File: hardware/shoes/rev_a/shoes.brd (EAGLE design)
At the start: 25.1 x 21.3 mm, 36 parts, among them J4 TC2030-JLINK-NL, Q1 MOSFET-NCHANNELXFDN-3, Q2 MOSFET-NCHANNELXFDN-3, Q3 MOSFET-NCHANNELXFDN-3, Q4 MOSFET-NCHANNELXFDN-3, U1 NRF51822QF, U2 ADXL362, X1 16MHz

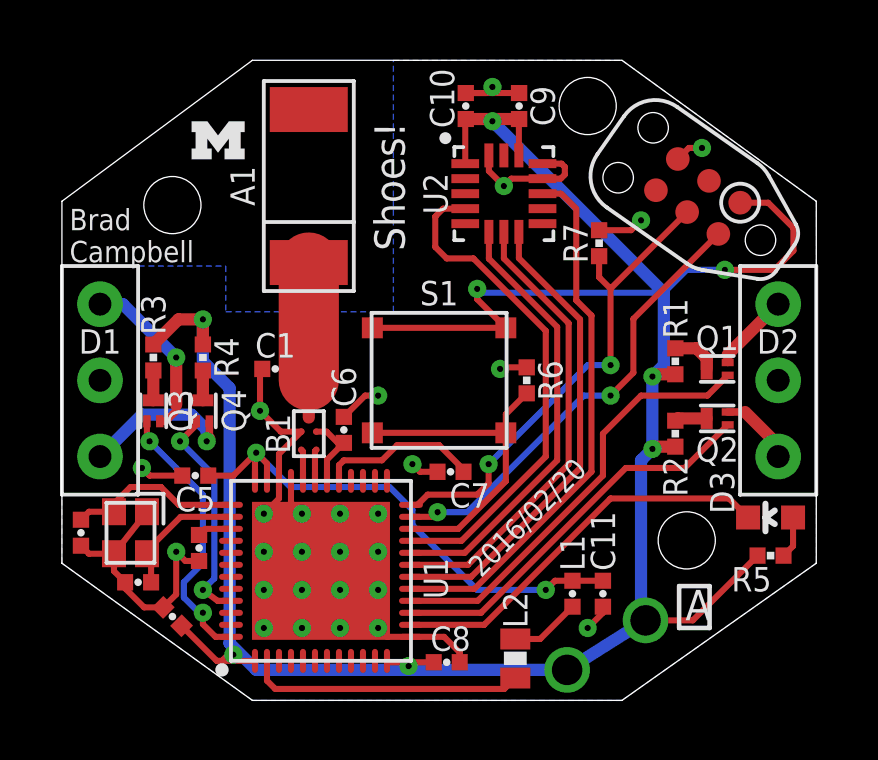
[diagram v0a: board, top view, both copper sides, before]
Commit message: board changes
added cap from power to ground
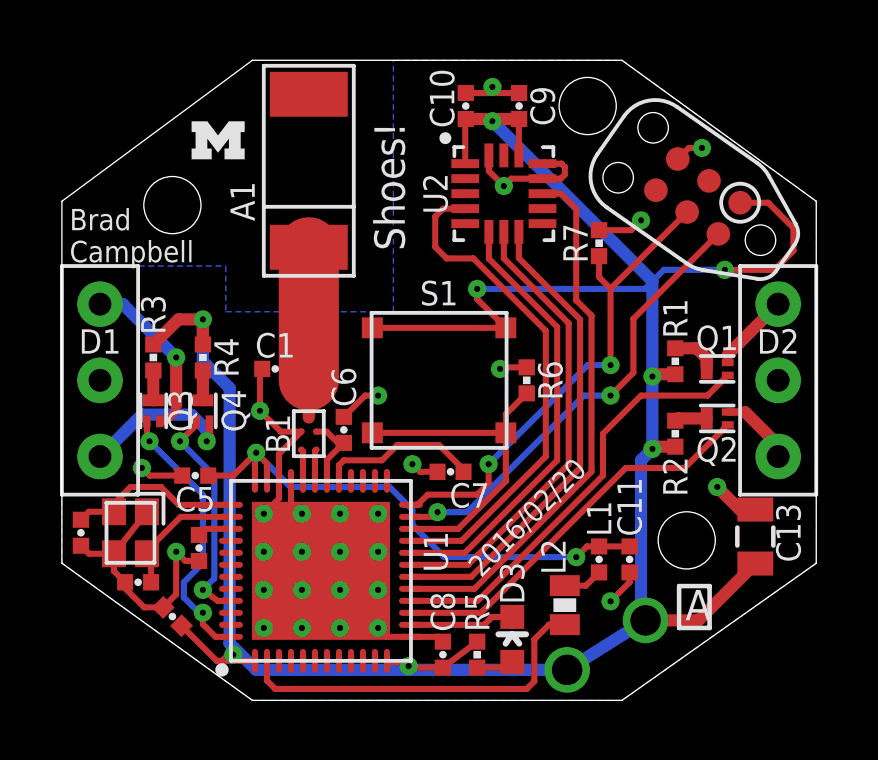
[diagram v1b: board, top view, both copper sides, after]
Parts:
- added C13: (no value), SparkFun-Capacitors:0805
- moved R5 10.3 mm to (1.27, -9.14), turned to 270 degrees
- moved D3 9.52 mm to (2.44, -8.64), turned to 0 degrees
- moved L2 2.43 mm to (4.19, -7.49)
- moved C11 1.45 mm to (6.35, -5.97)
- moved L1 1.45 mm to (5.33, -5.97)
- moved A1 0.51 mm to (-4.34, 6.99)
- moved C8 0.28 mm to (0.13, -9.14), turned to 90 degrees
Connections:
- net GND: now also C13.2
- net VCC: now also C13.1
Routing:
- net N$7: track 13.2 -> 3.48 mm
- net DCC: track 9.20 -> 12.4 mm
- net VCC: track 85.0 -> 86.0 mm
- net N$14: track 2.35 -> 1.33 mm
- net GND: track 36.0 -> 36.9 mm, vias 27 -> 28
- net N$11: track 6.14 -> 6.64 mm

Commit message: move antenna back
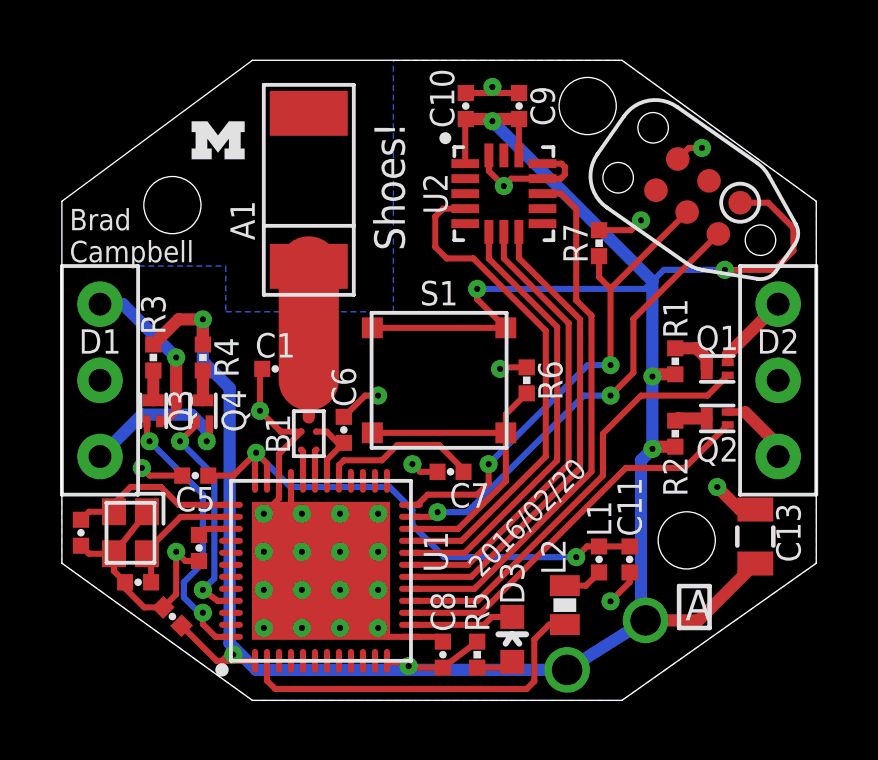
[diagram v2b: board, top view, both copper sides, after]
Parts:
- moved A1 0.64 mm to (-4.34, 6.35)
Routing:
- net N$11: track 6.64 -> 6.01 mm
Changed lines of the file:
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@@
 <attribute name="VALUE" x="-0.127" y="-9.144" size="1.016" layer="27" font="vector" ratio="12" rot="R270" align="bottom-center"/>
 </element>
-<element name="A1" library="chips" package="FRACTUS-ANTENNA-FR05-S1-N-0-102" value="FRACTUS-2.4GHZ-FR05-S1-N-0-102" x="-4.3434" y="6.985" smashed="yes" rot="R90">
-<attribute name="RICHARDSON_RFPD" value="FR05-S1-N-0102B" x="46.7106" y="-14.605" size="1.778" layer="27" rot="R90" display="off"/>
-<attribute name="NAME" x="-6.1434" y="5.969" size="0.8128" layer="25" font="vector" ratio="12" rot="R90" align="bottom-center"/>
+<element name="A1" library="chips" package="FRACTUS-ANTENNA-FR05-S1-N-0-102" value="FRACTUS-2.4GHZ-FR05-S1-N-0-102" x="-4.3434" y="6.35" smashed="yes" rot="R90">
+<attribute name="RICHARDSON_RFPD" value="FR05-S1-N-0102B" x="46.7106" y="-15.24" size="1.778" layer="27" rot="R90" display="off"/>
+<attribute name="NAME" x="-6.1434" y="5.334" size="0.8128" layer="25" font="vector" ratio="12" rot="R90" align="bottom-center"/>
 </element>
 <element name="L2" library="passives" package="0603_CAP" value="10uH" x="4.191" y="-7.493" smashed="yes" rot="R270">
@@
 <contactref element="A1" pad="1"/>
 <contactref element="C1" pad="1"/>
-<wire x1="-4.3434" y1="4.435" x2="-4.3434" y2="0" width="2.0066" layer="1"/>
+<wire x1="-4.3434" y1="3.8" x2="-4.3434" y2="0" width="2.0066" layer="1"/>
 <wire x1="-4.3434" y1="-1.241" x2="-4.3434" y2="-0.30353125" width="0.4064" layer="1"/>
 <wire x1="-4.3434" y1="-0.30353125" x2="-4.3434" y2="0" width="0.4064" layer="1"/>

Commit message: update pcb
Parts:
- added BAT1: BAT-CON-112TR, batteries:BAT-CON-112TR
- added TP1, TP2: TEST_POINT_0.020IN, headers:TESTPOINT_0.020IN
- added TP3, TP4, TP5, TP6, TP7: TPSQTP06SQ, testpad:TP06SQ
- moved B1 2.79 mm to (-4.34, 1.02)
- moved C1 1.91 mm to (-5.33, 2.29)
- moved J4 1.62 mm to (7.49, 7.27)
- moved C6 1.53 mm to (-3.05, -0.13)
- moved R6 0.38 mm to (2.92, -0.38)
- turned C7 to 0 degrees
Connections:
- new net N$1: TP2.TESTPOINT, U1.25
- net !ACCEL_CS: now also TP4.TP
- net ACCEL_INT: now also TP3.TP
- net GND: now also BAT1.PAD, TP1.TESTPOINT
- net MISO: now also TP6.TP
- net MOSI: now also TP7.TP
- net SCLK: now also TP5.TP
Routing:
- net N$1: track 0.00 -> 16.8 mm, vias 0 -> 2
- net VCC: track 86.0 -> 82.1 mm
- net N$11: track 6.01 -> 2.80 mm
- net VDD_PA: track 2.57 -> 5.53 mm
- net N$6: track 1.06 -> 3.85 mm
- net N$5: track 1.05 -> 3.85 mm
- net MISO: track 15.3 -> 17.4 mm, vias 0 -> 1
- net N$19: track 5.51 -> 4.03 mm
- net !ACCEL_CS: track 16.0 -> 17.4 mm, vias 0 -> 1
- net MOSI: track 14.7 -> 16.0 mm, vias 0 -> 1
- net ACCEL_INT: track 17.9 -> 19.2 mm, vias 0 -> 1
- net SWDIO/!RESET: track 15.2 -> 16.4 mm
- net SWDCLK: track 16.4 -> 17.5 mm
- net SCLK: track 16.8 -> 18.0 mm, vias 0 -> 1
- net GND: track 36.9 -> 36.2 mm, vias 28 -> 29

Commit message: new PCB preliminary working
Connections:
- removed net P25: U1.44
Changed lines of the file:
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@@
 <layer number="27" name="tValues" color="7" fill="1" visible="no" active="yes"/>
 <layer number="28" name="bValues" color="7" fill="1" visible="no" active="yes"/>
-<layer number="29" name="tStop" color="7" fill="3" visible="no" active="yes"/>
+<layer number="29" name="tStop" color="7" fill="3" visible="yes" active="yes"/>
 <layer number="30" name="bStop" color="7" fill="6" visible="no" active="yes"/>
 <layer number="31" name="tCream" color="7" fill="4" visible="no" active="yes"/>
@@
 <contactref element="R5" pad="1"/>
 <contactref element="J4" pad="1"/>
-<via x="4.2672" y="-9.652" extent="1-16" drill="1.016"/>
-<via x="6.8834" y="-8.001" extent="1-16" drill="1.016"/>
+<via x="4.2672" y="-9.652" extent="1-16" drill="1.016" alwaysstop="yes"/>
+<via x="6.8834" y="-8.001" extent="1-16" drill="1.016" alwaysstop="yes"/>
 <wire x1="-1.689" y1="-9.398" x2="-1.737" y2="-9.35" width="0.2032" layer="1"/>
 <contactref element="S1" pad="1"/>
@@
 <wire x1="1.502" y1="-8.15" x2="-0.937" y2="-8.15" width="0.2032" layer="1"/>
 </signal>
-<signal name="P25">
-<contactref element="U1" pad="44"/>
-</signal>
 <signal name="MAIN_SWITCH">
